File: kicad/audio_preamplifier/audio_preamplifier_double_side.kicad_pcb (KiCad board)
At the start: 2 copper layers, 26.2 x 15 mm, 23 parts, among them P2 CONN_01X03, P3 CONN_01X03, P4 CONN_01X02, U3 TL072

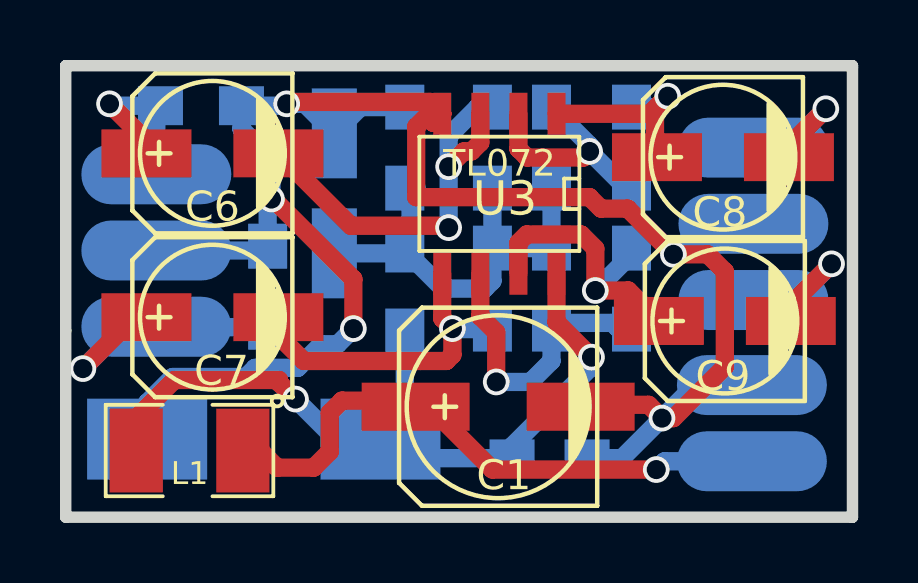
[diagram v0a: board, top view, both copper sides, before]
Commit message: new kicad version components in schematics
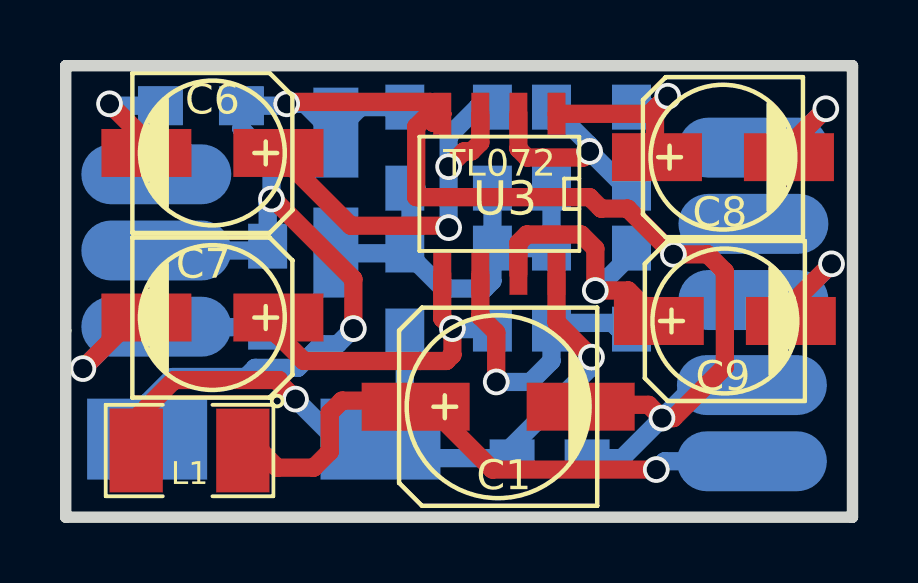
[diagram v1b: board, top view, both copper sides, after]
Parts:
- C1: value 100m -> 100m/25V
- C4, C8, C9: value 47m -> 47m/25V
- C5: value 2m2 -> 2m2/16V
- C6, C7: value 10m -> 10m/16V
- moved C5 0.06 mm to (197.7, 132.4), turned to 90 degrees
- turned C6 to 0 degrees
- turned C7 to 0 degrees
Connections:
- C5 pad 1: AGND -> /virtual_gnd
- C5 pad 2: /virtual_gnd -> AGND
- C6 pad 1: right_in -> Net-(C6-Pad1)
- C6 pad 2: Net-(C6-Pad2) -> right_in
- C7 pad 1: left_in -> Net-(C7-Pad1)
- C7 pad 2: Net-(C7-Pad2) -> left_in
- R12 pad 1: Net-(C6-Pad2) -> Net-(C6-Pad1)
- R13 pad 1: Net-(C7-Pad2) -> Net-(C7-Pad1)
- U3 pad 3: Net-(C6-Pad2) -> Net-(C6-Pad1)
- U3 pad 5: Net-(C7-Pad2) -> Net-(C7-Pad1)
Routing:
- net Net-(C6-Pad2): track 14.0 -> 0.00 mm, vias 2 -> 0
- net Net-(C6-Pad1): track 0.00 -> 14.0 mm, vias 0 -> 2
- net Net-(C7-Pad2): track 11.2 -> 0.00 mm, vias 1 -> 0
- net Net-(C7-Pad1): track 0.00 -> 11.2 mm, vias 0 -> 1
